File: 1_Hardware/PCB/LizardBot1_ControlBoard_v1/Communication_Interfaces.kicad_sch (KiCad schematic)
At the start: 0 parts

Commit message: Added Communication_Interfaces schematic
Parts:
- added J601: JST-PH-4-Male, symbol Connector_Generic:Conn_01x04
- added J602: Conn_02x04_Top_Bottom, symbol Connector_Generic:Conn_02x04_Top_Bottom
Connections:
- new net +3V3: J601.3 (Pin_3), J602.1 (Pin_1), J602.7 (Pin_7)
- new net GND: J601.4 (Pin_4), J602.4 (Pin_4), J602.8 (Pin_8)
- new net MCU_RXD0: J601.2 (Pin_2)
- new net MCU_SCL: J602.3 (Pin_3), J602.6 (Pin_6)
- new net MCU_SDA: J602.2 (Pin_2), J602.5 (Pin_5)
- new net MCU_TXD0: J601.1 (Pin_1)
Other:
- note added: "(!) Review signal order at PCB design (!)"
- note added: "I2C & OLED Connector"
- note added: "UART Connector"

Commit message: PCB schematics revision
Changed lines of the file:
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@@
 	(wire
 		(pts
-			(xy 63.5 52.07) (xy 67.31 52.07)
+			(xy 133.35 186.69) (xy 152.4 186.69)
+		)
+		(stroke
+			(width 0)
+			(type default)
+		)
+	)
+	(wire
+		(pts
+			(xy 53.34 52.07) (xy 67.31 52.07)
 		)
 		(stroke
@@
 	(wire
 		(pts
-			(xy 154.94 52.07) (xy 158.75 52.07)
-		)
-		(stroke
-			(width 0)
-			(type default)
-		)
-	)
-	(wire
-		(pts
 			(xy 120.65 59.69) (xy 142.24 59.69)
 		)
@@
 	(wire
 		(pts
-			(xy 138.43 57.15) (xy 142.24 57.15)
-		)
-		(stroke
-			(width 0)
-			(type default)
-		)
-	)
-	(wire
-		(pts
-			(xy 138.43 54.61) (xy 142.24 54.61)
+			(xy 125.73 57.15) (xy 142.24 57.15)
+		)
+		(stroke
+			(width 0)
+			(type default)
+		)
+	)
+	(wire
+		(pts
+			(xy 125.73 54.61) (xy 142.24 54.61)
+		)
+		(stroke
+			(width 0)
+			(type default)
+		)
+	)
+	(wire
+		(pts
+			(xy 154.94 54.61) (xy 171.45 54.61)
 		)
 		(stroke
@@
 	(wire
 		(pts
+			(xy 154.94 52.07) (xy 171.45 52.07)
+		)
+		(stroke
+			(width 0)
+			(type default)
+		)
+	)
+	(wire
+		(pts
+			(xy 133.35 184.15) (xy 152.4 184.15)
+		)
+		(stroke
+			(width 0)
+			(type default)
+		)
+	)
+	(wire
+		(pts
 			(xy 44.45 49.53) (xy 44.45 57.15)
 		)
@@
 	(wire
 		(pts
+			(xy 120.65 49.53) (xy 120.65 52.07)
+		)
+		(stroke
+			(width 0)
+			(type default)
+		)
+	)
+	(wire
+		(pts
+			(xy 133.35 179.07) (xy 152.4 179.07)
+		)
+		(stroke
+			(width 0)
+			(type default)
+		)
+	)
+	(wire
+		(pts
+			(xy 133.35 181.61) (xy 152.4 181.61)
+		)
+		(stroke
+			(width 0)
+			(type default)
+		)
+	)
+	(polyline
+		(pts
+			(xy 148.59 63.5) (xy 148.59 83.82)
+		)
+		(stroke
+			(width 0)
+			(type dash)
+		)
+	)
+	(wire
+		(pts
 			(xy 154.94 57.15) (xy 176.53 57.15)
 		)
@@
 	(wire
 		(pts
-			(xy 120.65 49.53) (xy 120.65 52.07)
+			(xy 120.65 62.23) (xy 120.65 59.69)
+		)
+		(stroke
+			(width 0)
+			(type default)
+		)
+	)
+	(wire
+		(pts
+			(xy 44.45 62.23) (xy 44.45 59.69)
+		)
+		(stroke
+			(width 0)
+			(type default)
+		)
+	)
+	(wire
+		(pts
+			(xy 154.94 59.69) (xy 176.53 59.69)
+		)
+		(stroke
+			(width 0)
+			(type default)
+		)
+	)
+	(wire
+		(pts
+			(xy 53.34 54.61) (xy 67.31 54.61)
+		)
+		(stroke
+			(width 0)
+			(type default)
+		)
+	)
+	(wire
+		(pts
+			(xy 176.53 62.23) (xy 176.53 59.69)
 		)
 		(stroke
@@
 	(polyline
 		(pts
-			(xy 148.59 63.5) (xy 148.59 83.82)
+			(xy 148.59 30.48) (xy 148.59 43.18)
 		)
 		(stroke
 			(width 0)
 			(type dash)
-		)
-	)
-	(wire
-		(pts
-			(xy 120.65 62.23) (xy 120.65 59.69)
-		)
-		(stroke
-			(width 0)
-			(type default)
-		)
-	)
-	(wire
-		(pts
-			(xy 44.45 62.23) (xy 44.45 59.69)
-		)
-		(stroke
-			(width 0)
-			(type default)
-		)
-	)
-	(wire
-		(pts
-			(xy 154.94 59.69) (xy 176.53 59.69)
-		)
-		(stroke
-			(width 0)
-			(type default)
-		)
-	)
-	(wire
-		(pts
-			(xy 63.5 54.61) (xy 67.31 54.61)
-		)
-		(stroke
-			(width 0)
-			(type default)
-		)
-	)
-	(wire
-		(pts
-			(xy 176.53 62.23) (xy 176.53 59.69)
-		)
-		(stroke
-			(width 0)
-			(type default)
-		)
-	)
-	(polyline
-		(pts
-			(xy 148.59 30.48) (xy 148.59 43.18)
-		)
-		(stroke
-			(width 0)
-			(type dash)
-		)
-	)
-	(wire
-		(pts
-			(xy 154.94 54.61) (xy 158.75 54.61)
-		)
-		(stroke
-			(width 0)
-			(type default)
 		)
 	)
@@
 		)
 	)
+	(label "MCU_SDA"
+		(at 171.45 52.07 180)
+		(fields_autoplaced yes)
+		(effects
+			(font
+				(size 1.27 1.27)
+			)
+			(justify right bottom)
+		)
+	)
+	(label "MCU_SDA"
+		(at 125.73 54.61 0)
+		(fields_autoplaced yes)
+		(effects
+			(font
+				(size 1.27 1.27)
+			)
+			(justify left bottom)
+		)
+	)
+	(label "MCU_SCL"
+		(at 125.73 57.15 0)
+		(fields_autoplaced yes)
+		(effects
+			(font
+				(size 1.27 1.27)
+			)
+			(justify left bottom)
+		)
+	)
+	(label "MCU_SCL"
+		(at 171.45 54.61 180)
+		(fields_autoplaced yes)
+		(effects
+			(font
+				(size 1.27 1.27)
+			)
+			(justify right bottom)
+		)
+	)
+	(label "MCU_TXD0"
+		(at 53.34 52.07 0)
+		(fields_autoplaced yes)
+		(effects
+			(font
+				(size 1.27 1.27)
+			)
+			(justify left bottom)
+		)
+	)
+	(label "MCU_TXD0"
+		(at 133.35 181.61 0)
+		(fields_autoplaced yes)
+		(effects
+			(font
+				(size 1.27 1.27)
+			)
+			(justify left bottom)
+		)
+	)
+	(label "MCU_SCL"
+		(at 133.35 186.69 0)
+		(fields_autoplaced yes)
+		(effects
+			(font
+				(size 1.27 1.27)
+			)
+			(justify left bottom)
+		)
+	)
+	(label "MCU_RXD0"
+		(at 53.34 54.61 0)
+		(fields_autoplaced yes)
+		(effects
+			(font
+				(size 1.27 1.27)
+			)
+			(justify left bottom)
+		)
+	)
+	(label "MCU_RXD0"
+		(at 133.35 179.07 0)
+		(fields_autoplaced yes)
+		(effects
+			(font
+				(size 1.27 1.27)
+			)
+			(justify left bottom)
+		)
+	)
+	(label "MCU_SDA"
+		(at 133.35 184.15 0)
+		(fields_autoplaced yes)
+		(effects
+			(font
+				(size 1.27 1.27)
+			)
+			(justify left bottom)
+		)
+	)
 	(hierarchical_label "MCU_SDA"
 		(shape bidirectional)
-		(at 158.75 52.07 0)
+		(at 152.4 184.15 0)
+		(fields_autoplaced yes)
+		(effects
+			(font
+				(size 1.27 1.27)
+			)
+			(justify left)
+		)
+	)
+	(hierarchical_label "MCU_RXD0"
+		(shape input)
+		(at 152.4 179.07 0)
 		(fields_autoplaced yes)
 		(effects
@@
 	(hierarchical_label "MCU_SCL"
 		(shape bidirectional)
-		(at 158.75 54.61 0)
+		(at 152.4 186.69 0)
 		(fields_autoplaced yes)
 		(effects
@@
 		)
 	)
-	(hierarchical_label "MCU_SCL"
-		(shape bidirectional)
-		(at 138.43 57.15 180)
-		(fields_autoplaced yes)
-		(effects
-			(font
-				(size 1.27 1.27)
-			)
-			(justify right)
-		)
-	)
 	(hierarchical_label "MCU_TXD0"
-		(shape input)
-		(at 63.5 52.07 180)
-		(fields_autoplaced yes)
-		(effects
-			(font
-				(size 1.27 1.27)
-			)
-			(justify right)
-		)
-	)
-	(hierarchical_label "MCU_RXD0"
 		(shape output)
-		(at 63.5 54.61 180)
-		(fields_autoplaced yes)
-		(effects
-			(font
-				(size 1.27 1.27)
-			)
-			(justify right)
-		)
-	)
-	(hierarchical_label "MCU_SDA"
-		(shape bidirectional)
-		(at 138.43 54.61 180)
-		(fields_autoplaced yes)
-		(effects
-			(font
-				(size 1.27 1.27)
-			)
-			(justify right)
-		)
-	)
+		(at 152.4 181.61 0)
+		(fields_autoplaced yes)
+		(effects
+			(font
+				(size 1.27 1.27)
+			)
+			(justify left)
+		)
+	)

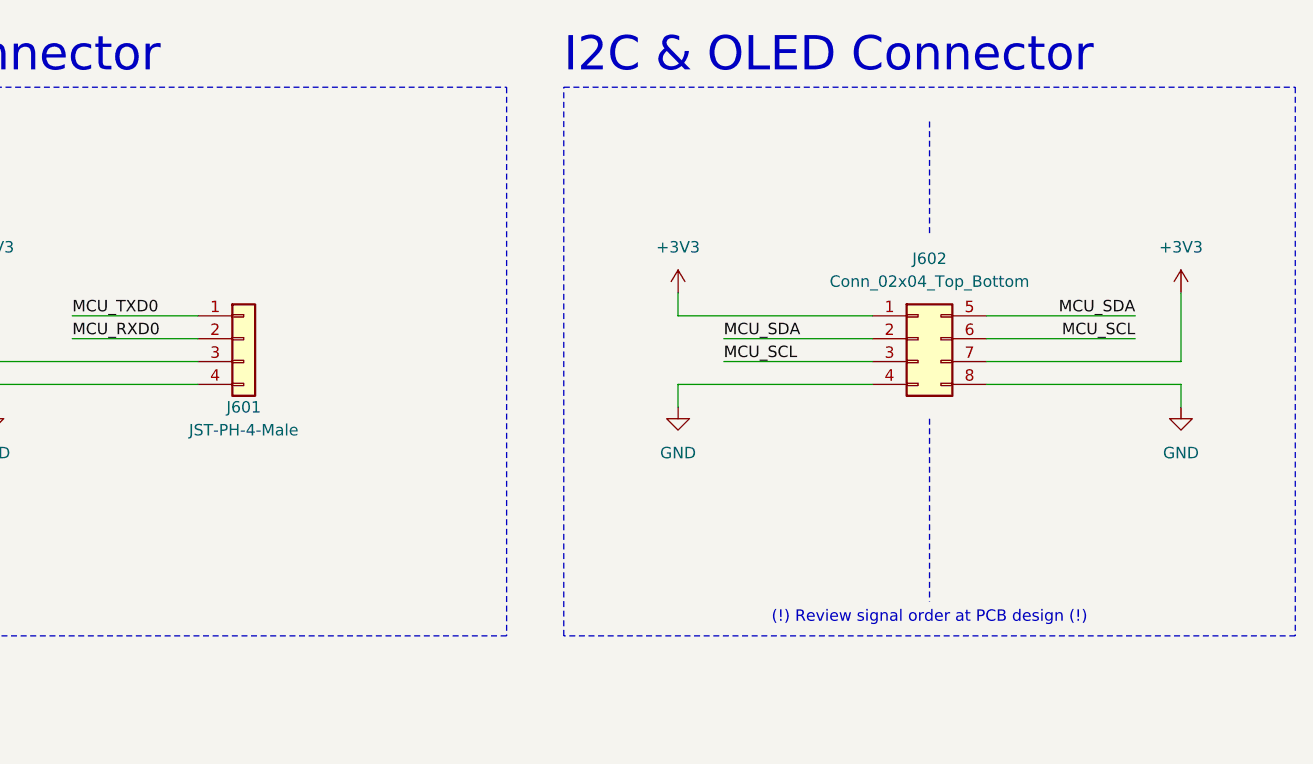
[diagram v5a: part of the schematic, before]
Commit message: Updated schematics. Assigned footprints. Added BOM to /4_Docs.
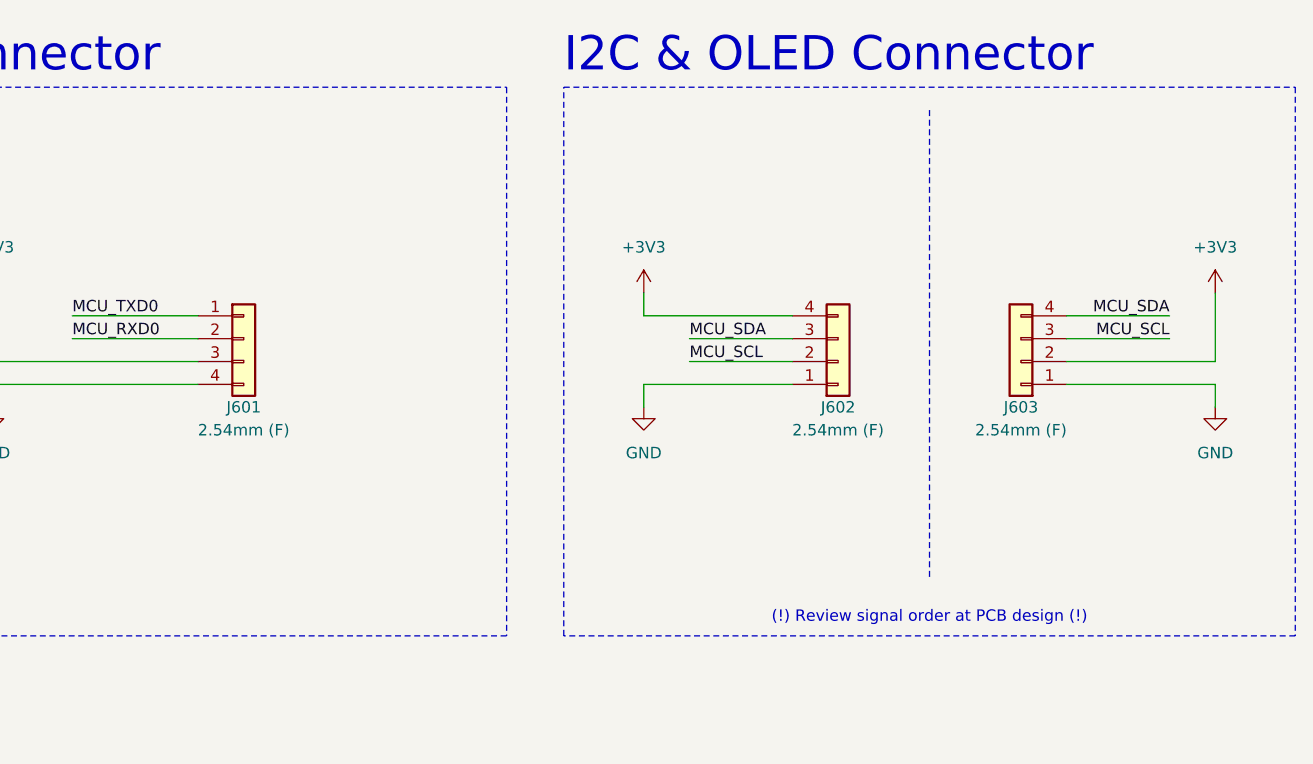
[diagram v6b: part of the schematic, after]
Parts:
- removed J602: Conn_02x04_Top_Bottom, symbol Connector_Generic:Conn_02x04_Top_Bottom
- added J602, J603: 2.54mm (F), Connector_PinHeader_2.54mm:PinHeader_1x04_P2.54mm_Vertical, symbol Connector_Generic:Conn_01x04
- J601: value JST-PH-4-Male -> 2.54mm (F); footprint (none) -> Connector_PinHeader_2.54mm:PinHeader_1x04_P2.54mm_Vertical
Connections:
- net +3V3: now also J602.4 (Pin_4), J603.2 (Pin_2)
- net GND: now also J602.1 (Pin_1), J603.1 (Pin_1)
- net MCU_SCL: now also J602.2 (Pin_2), J603.3 (Pin_3)
- net MCU_SDA: now also J602.3 (Pin_3), J603.4 (Pin_4)

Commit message: Finished robot controller PCB. Generated production files.
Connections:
- net +3V3: now also J601.2 (Pin_2), J602.2 (Pin_2); no longer J601.3 (Pin_3), J602.4 (Pin_4)
- net GND: now also J601.1 (Pin_1); no longer J601.4 (Pin_4)
- net MCU_RXD0: now also J601.4 (Pin_4); no longer J601.2 (Pin_2)
- net MCU_SCL: now also J602.3 (Pin_3); no longer J602.2 (Pin_2)
- net MCU_SDA: now also J602.4 (Pin_4); no longer J602.3 (Pin_3)
- net MCU_TXD0: now also J601.3 (Pin_3); no longer J601.1 (Pin_1)
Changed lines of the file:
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@@
-	(wire
-		(pts
-			(xy 53.34 52.07) (xy 67.31 52.07)
-		)
-		(stroke
-			(width 0)
-			(type default)
-		)
-	)
-	(wire
-		(pts
-			(xy 116.84 52.07) (xy 133.35 52.07)
-		)
-		(stroke
-			(width 0)
-			(type default)
-		)
-	)
 	(wire
 		(pts
@@
 	(wire
 		(pts
-			(xy 121.92 57.15) (xy 133.35 57.15)
-		)
-		(stroke
-			(width 0)
-			(type default)
-		)
-	)
-	(wire
-		(pts
-			(xy 121.92 54.61) (xy 133.35 54.61)
+			(xy 44.45 57.15) (xy 67.31 57.15)
+		)
+		(stroke
+			(width 0)
+			(type default)
+		)
+	)
+	(wire
+		(pts
+			(xy 116.84 57.15) (xy 133.35 57.15)
+		)
+		(stroke
+			(width 0)
+			(type default)
+		)
+	)
+	(wire
+		(pts
+			(xy 67.31 52.07) (xy 53.34 52.07)
+		)
+		(stroke
+			(width 0)
+			(type default)
+		)
+	)
+	(wire
+		(pts
+			(xy 133.35 54.61) (xy 121.92 54.61)
 		)
 		(stroke
@@
 	(wire
 		(pts
-			(xy 44.45 57.15) (xy 67.31 57.15)
-		)
-		(stroke
-			(width 0)
-			(type default)
-		)
-	)
-	(wire
-		(pts
 			(xy 163.83 52.07) (xy 175.26 52.07)
 		)
@@
 	(wire
 		(pts
-			(xy 116.84 49.53) (xy 116.84 52.07)
+			(xy 116.84 49.53) (xy 116.84 57.15)
 		)
 		(stroke
@@
 	(wire
 		(pts
+			(xy 133.35 52.07) (xy 121.92 52.07)
+		)
+		(stroke
+			(width 0)
+			(type default)
+		)
+	)
+	(wire
+		(pts
 			(xy 116.84 62.23) (xy 116.84 59.69)
 		)
@@
 	(wire
 		(pts
-			(xy 53.34 54.61) (xy 67.31 54.61)
+			(xy 67.31 54.61) (xy 53.34 54.61)
 		)
 		(stroke
@@
 	)
 	(label "MCU_SDA"
+		(at 121.92 52.07 0)
+		(fields_autoplaced yes)
+		(effects
+			(font
+				(size 1.27 1.27)
+			)
+			(justify left bottom)
+		)
+	)
+	(label "MCU_SCL"
 		(at 121.92 54.61 0)
-		(fields_autoplaced yes)
-		(effects
-			(font
-				(size 1.27 1.27)
-			)
-			(justify left bottom)
-		)
-	)
-	(label "MCU_SCL"
-		(at 121.92 57.15 0)
 		(fields_autoplaced yes)
 		(effects
@@
 	)
 	(label "MCU_TXD0"
-		(at 53.34 52.07 0)
-		(fields_autoplaced yes)
-		(effects
-			(font
-				(size 1.27 1.27)
-			)
-			(justify left bottom)
-		)
-	)
-	(label "MCU_TXD0"
 		(at 133.35 181.61 0)
 		(fields_autoplaced yes)
@@
 		)
 	)
-	(label "MCU_RXD0"
+	(label "MCU_TXD0"
 		(at 53.34 54.61 0)
 		(fields_autoplaced yes)
@@
 	(label "MCU_SDA"
 		(at 133.35 184.15 0)
+		(fields_autoplaced yes)
+		(effects
+			(font
+				(size 1.27 1.27)
+			)
+			(justify left bottom)
+		)
+	)
+	(label "MCU_RXD0"
+		(at 53.34 52.07 0)
 		(fields_autoplaced yes)
 		(effects
@@
 	(symbol
 		(lib_id "Connector_Generic:Conn_01x04")
-		(at 72.39 54.61 0)
+		(at 72.39 57.15 0)
+		(mirror x)
 		(unit 1)
 		(exclude_from_sim no)
@@
 		)
 		(property "Footprint" "Connector_PinHeader_2.54mm:PinHeader_1x04_P2.54mm_Vertical"
-			(at 72.39 54.61 0)
+			(at 72.39 57.15 0)
 			(effects
 				(font
@@
 		)
 		(property "Datasheet" "~"
-			(at 72.39 54.61 0)
+			(at 72.39 57.15 0)
 			(effects
 				(font
@@
 		)
 		(property "Description" "Generic connector, single row, 01x04, script generated (kicad-library-utils/schlib/autogen/connector/)"
-			(at 72.39 54.61 0)
-			(effects
-				(font
+			(at 72.39 57.15 0)
+			(effects
+				(font
